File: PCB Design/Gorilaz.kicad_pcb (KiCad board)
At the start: 2 copper layers, 100 x 86 mm, 20 parts, among them J1 Conn_01x13, J2 Conn_01x13, J3 Conn_01x13, J4 Conn_01x13, J7 Conn_01x13, J8 Conn_01x13, M1 MountingHole_6.4mm_M6, M3 MountingHole_4.3mm_M4, M4 MountingHole_4.3mm_M4

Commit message: schema update
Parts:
- removed BZ1: Buzzer, Buzzer_Beeper:Buzzer_TDK_PS1240P02BT_D12.2mm_H6.5mm
- removed R1, R2, R3: R_US, Keebio-Parts:Resistor-Hybrid
- added C1: 100n, Capacitor_SMD:C_0402_1005Metric, F.Cu at (169.9, 119.6)
- added C17: 100n, Capacitor_SMD:C_0402_1005Metric, F.Cu at (124.0, 103.5)
- added C5: 4u7, Capacitor_SMD:C_0402_1005Metric, F.Cu at (125.5, 82.0)
- added C6: 4u7, Capacitor_SMD:C_0402_1005Metric, F.Cu at (129.3, 85.8)
- added C7: 4u7, Capacitor_SMD:C_0402_1005Metric, F.Cu at (120.0, 86.5)
- added C8: 100n, Capacitor_SMD:C_0402_1005Metric, F.Cu at (126.5, 113.0)
- added D2: LED_NUM, LED_SMD:LED_1206_3216Metric, F.Cu at (142.1, 140.0)
- added D3: LED_SCR, LED_SMD:LED_1206_3216Metric, F.Cu at (153.1, 140.5)
- added D5: BSD3C051V, Diode_SMD:D_SOD-323, F.Cu at (170.5, 122.0)
- added F1: 750 mA, Fuse:Fuse_0603_1608Metric, F.Cu at (160.5, 119.8)
- added J5: HRO_TYPE-C-31-M-14, Connector_USB:USB_C_Receptacle_HRO_TYPE-C-31-M-12, F.Cu at (165.2, 130.4)
- added J6: Battery, Local:Molex_Pico-EZmate_78171-0002_1x02-1MP_P1.20mm_Vertical, F.Cu at (125.2, 128.1)
- added J9: TC2030_SWD, Local:CON_TC2030_outlined, F.Cu at (156.4, 80.2)
- added L1: BLM15PX121SN1D, Inductor_SMD:L_0402_1005Metric, F.Cu at (160.5, 123.5)
- added L2: BLM15PX121SN1D, Inductor_SMD:L_0402_1005Metric, F.Cu at (170.0, 124.0)
- added LED2: orange, LED_SMD:LED_0402_1005Metric, F.Cu at (129.0, 91.5)
- added Q2: 2N7002, Package_TO_SOT_SMD:SOT-23, F.Cu at (130.9, 78.5)
- added R10: 1k5, Resistor_SMD:R_0402_1005Metric, F.Cu at (129.0, 89.0)
- added R11: 47k, Resistor_SMD:R_0402_1005Metric, F.Cu at (124.5, 82.0)
- added R12: 1k5, Resistor_SMD:R_0402_1005Metric, F.Cu at (129.5, 84.5)
- added R13: 3k9, Resistor_SMD:R_0402_1005Metric, F.Cu at (122.5, 82.0)
- added R15: 100R, Resistor_SMD:R_0402_1005Metric, F.Cu at (124.5, 122.5)
- added R17: 1k, Resistor_SMD:R_0402_1005Metric, F.Cu at (130.0, 121.0)
- added R18: 5k1, Resistor_SMD:R_0402_1005Metric, F.Cu at (131.5, 101.0)
- added R19: 5k1, Resistor_SMD:R_0402_1005Metric, F.Cu at (131.5, 103.0)
- added R20: 10k, Resistor_SMD:R_0805_2012Metric, F.Cu at (128.6, 136.5)
- added R21: 10k, Resistor_SMD:R_0805_2012Metric, F.Cu at (139.6, 136.5)
- added R22: 10k, Resistor_SMD:R_0805_2012Metric, F.Cu at (151.6, 137.5)
- added R5: 5k1, Resistor_SMD:R_0402_1005Metric, F.Cu at (166.8, 123.7)
- added R6: 10k, Resistor_SMD:R_0402_1005Metric, F.Cu at (127.9, 78.0)
- added R7: 100R, Resistor_SMD:R_0402_1005Metric, F.Cu at (125.9, 77.5)
- added R8: 100k, Resistor_SMD:R_0402_1005Metric, F.Cu at (132.0, 74.5)
- added R9: 10k, Resistor_SMD:R_0402_1005Metric, F.Cu at (120.0, 85.5)
- added SW1: PWR, Mastarlib:SW_MSK12C02-HB, F.Cu at (121.5, 57.5)
- added SW4: RST, Button_Switch_SMD:SW_SPST_SKQG_WithStem, F.Cu at (132.9, 58.1)
- added U1: SRV05-4, Package_TO_SOT_SMD:SOT-23-6, F.Cu at (164.6, 114.0)
- added U10: MAX17048, Local:DFN-8-1EP_2x2mm_P0.5mm_EP0.7x1.3mm, F.Cu at (127.5, 102.2)
- added U3: BQ24075, Package_DFN_QFN:VQFN-16-1EP_3x3mm_P0.5mm_EP1.6x1.6mm, F.Cu at (124.8, 86.1)
- added U4: DW01A, Package_TO_SOT_SMD:SOT-23-6, F.Cu at (127.0, 116.4)
- added U5: FS8205, Package_TO_SOT_SMD:SOT-23-6, F.Cu at (127.0, 122.4)
- added U8: nRF52840_moko_mk08, Mastarlib:nRF52840_moko_mk08, F.Cu at (169.6, 71.3)
- D1: footprint LED_THT:LED_D3.0mm -> LED_SMD:LED_1206_3216Metric
- D2, D3, D4, H1: moved to B.Cu
- H2, M1, M3, M4: moved to F.Cu
- J1, J2: footprint kinesisMod_board_connectors:Molex_0039532135 -> Local:Molex_0039532135; moved to F.Cu
- J3, J4: footprint kinesisMod_board_connectors:Molex_039532134 -> Local:Molex_0039532135; moved to F.Cu
- J7, J8: footprint kinx:39-53-2135 -> Local:Molex_0039532135; moved to F.Cu
- R4: value R_US -> 5k1; footprint Keebio-Parts:Resistor-Hybrid -> Resistor_SMD:R_0402_1005Metric; moved to F.Cu
- moved J3 88.7 mm to (106.0, 107.0)
- moved J4 86.8 mm to (190.0, 107.0)
- moved J1 84.8 mm to (106.0, 60.0)
- moved J2 83.1 mm to (190.0, 60.0)
- moved M3 81.7 mm to (107.5, 94.6), turned to 180 degrees
- moved M4 79.5 mm to (188.1, 94.6), turned to 180 degrees
- moved J7 73.1 mm to (112.0, 123.0)
- moved J8 71.6 mm to (184.0, 123.0)
- moved D4 28.5 mm to (134.1, 129.4), turned to 180 degrees
- moved D2 11.5 mm to (154.1, 129.4), turned to 180 degrees
- moved D1 10.6 mm to (133.6, 140.0)
- moved D3 8.48 mm to (144.1, 129.4), turned to 180 degrees
- moved R4 2.08 mm to (163.9, 123.7)
- moved H1 1.08 mm to (147.8, 103.0), turned to 180 degrees
- moved H2 1.08 mm to (147.8, 57.0), turned to 0 degrees
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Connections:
- net /COL_0 renamed col0
- net /COL_1 renamed col1
- net /COL_2 renamed col2
- net /COL_3 renamed col3
- net /COL_4 renamed col4
- net /COL_5 renamed col5
- net /COL_6 renamed col6
- net /ROW_12 renamed row12
- net /ROW_13 renamed row13
- net /ROW_14 renamed row14
- net /ROW_2 renamed row2
- net /ROW_3 renamed row3
- net /ROW_4 renamed row4
- net /ROW_5 renamed row5
- net /ROW_6 renamed row6
- net /ROW_7 renamed row7
- net /ROW_8 renamed row8
- net /ROW_9 renamed row9
- J3 pad 1: /ROW_10 -> row10
- J3 pad 8: /ROW_11 -> row11
- J4 pad 6: /ROW_0 -> row0
- J4 pad 7: /ROW_1 -> row1
- R4 pad 1: Net-(D4-A) -> GNDPWR
- R4 pad 2: /LED_KEYPAD -> Net-(J5-CC1)
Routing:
- net +BATT: track 0.00 -> 32.0 mm, vias 0 -> 2
- net GND: track 0.00 -> 17.8 mm
- net Net-(U4-VDD): track 0.00 -> 15.1 mm
- net SYSOFF: track 0.00 -> 14.5 mm, vias 0 -> 2
- net Net-(J6-Pin_2): track 0.00 -> 13.9 mm
- net USB-D+: track 0.00 -> 12.1 mm
- net USB-D-: track 0.00 -> 11.5 mm
- net SCL: track 0.00 -> 11.4 mm
- net VBUS: track 0.00 -> 11.2 mm
- net Earth: track 0.00 -> 10.2 mm
- net SDA: track 0.00 -> 9.99 mm
- net +5V: track 0.00 -> 8.71 mm
- net Net-(U4-CSI): track 0.00 -> 7.45 mm
- net +3.3V: track 0.00 -> 5.02 mm, vias 0 -> 2
- net Net-(D1-A): track 4.50 -> 0.00 mm
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
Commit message: v0
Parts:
- removed the D2 at (154.1, 129.4)
- removed the D3 at (144.1, 129.4)
- removed D4: LED_ALT, LED_THT:LED_D3.0mm
- removed J9: TC2030_SWD, Local:CON_TC2030_outlined
- D1, D2, D3: moved to B.Cu
- H1: moved to F.Cu
- moved SW4 36.0 mm to (157.8, 84.0)
- moved SW1 28.4 mm to (130.5, 84.4), turned to 90 degrees
- moved R20 22.3 mm to (141.4, 118.2)
- moved R15 22.0 mm to (130.2, 101.3)
- moved R17 22.0 mm to (135.7, 99.8)
- moved U5 22.0 mm to (132.7, 101.1)
- moved R21 21.8 mm to (151.4, 118.2)
- moved R22 21.7 mm to (161.4, 118.2)
- moved U4 20.8 mm to (132.6, 96.4)
- moved D3 20.5 mm to (161.3, 121.7), turned to 180 degrees
- moved D2 20.5 mm to (151.3, 121.7), turned to 180 degrees
- moved C8 20.4 mm to (132.2, 93.3)
- moved D1 19.9 mm to (141.3, 121.7), turned to 180 degrees
- moved R8 18.9 mm to (136.4, 92.9)
- moved U1 16.9 mm to (173.2, 99.5), turned to -90 degrees
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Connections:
- U8 pad 1: LED_CAPS_LOCK -> col5
- U8 pad 13: unconnected-(U8-P0.04-A-Pad13) -> LED_CAPS_LOCK
- U8 pad 14: unconnected-(U8-P0.06-Pad14) -> LED_NUM_LOCK
- U8 pad 15: unconnected-(U8-P0.11-Pad15) -> LED_SCROLL_LOCK
- U8 pad 16: unconnected-(U8-P0.08-Pad16) -> LED_KEYPAD
- U8 pad 17: unconnected-(U8-P0.09-LF-NFC-Pad17) -> col6
- U8 pad 18: unconnected-(U8-P0.10-LF-NFC-Pad18) -> col4
- U8 pad 2: LED_NUM_LOCK -> row10
- U8 pad 21: col0 -> col3
- U8 pad 22: col1 -> col2
- U8 pad 23: col2 -> col1
- U8 pad 24: col3 -> row0
- U8 pad 25: col4 -> row1
- U8 pad 26: col5 -> row2
- U8 pad 28: col6 -> row3
- U8 pad 29: unconnected-(U8-P0.20-Pad29) -> row4
- U8 pad 3: LED_SCROLL_LOCK -> row9
- U8 pad 30: unconnected-(U8-P0.21-Pad30) -> row5
- U8 pad 31: unconnected-(U8-P0.22-Pad31) -> row14
- U8 pad 32: unconnected-(U8-P0.23-Pad32) -> row13
- U8 pad 33: unconnected-(U8-P0.24-Pad33) -> col0
- U8 pad 34: unconnected-(U8-P0.25-Pad34) -> row12
- U8 pad 35: row0 -> unconnected-(U8-P1.10-LF-Pad35)
- U8 pad 36: row1 -> unconnected-(U8-P1.11-LF-Pad36)
- U8 pad 37: row2 -> unconnected-(U8-P1.12-LF-Pad37)
- U8 pad 38: row3 -> unconnected-(U8-P1.13-LF-Pad38)
- U8 pad 4: LED_KEYPAD -> row11
- U8 pad 40: row4 -> row6
- U8 pad 41: row5 -> unconnected-(U8-P1.15-LF-Pad41)
- U8 pad 44: row6 -> unconnected-(U8-P1.08-Pad44)
- U8 pad 45: row7 -> unconnected-(U8-P1.09-Pad45)
- U8 pad 5: unconnected-(U8-P0.30-LF-A-Pad5) -> row7
- U8 pad 50: row8 -> unconnected-(U8-P1.01-LF-Pad50)
- U8 pad 51: row9 -> unconnected-(U8-P1.02-LF-Pad51)
- U8 pad 52: row10 -> unconnected-(U8-P1.03-LF-Pad52)
- U8 pad 53: row11 -> unconnected-(U8-P1.04-LF-Pad53)
- U8 pad 54: row12 -> unconnected-(U8-P1.05-LF-Pad54)
- U8 pad 55: row13 -> unconnected-(U8-P1.06-LF-Pad55)
- U8 pad 56: row14 -> unconnected-(U8-P1.07-LF-Pad56)
- U8 pad 6: unconnected-(U8-P0.31-LF-A-Pad6) -> row8
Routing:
- net col5: track 0.00 -> 261.1 mm, vias 0 -> 3
- net col1: track 0.00 -> 171.3 mm, vias 0 -> 4
- net col2: track 0.00 -> 168.4 mm, vias 0 -> 4
- net col0: track 0.00 -> 168.3 mm, vias 0 -> 4
- net col4: track 0.00 -> 166.0 mm, vias 0 -> 4
- net col3: track 0.00 -> 162.8 mm, vias 0 -> 4
- net row14: track 0.00 -> 156.7 mm, vias 0 -> 8
- net row13: track 0.00 -> 153.9 mm, vias 0 -> 6
- net row12: track 0.00 -> 129.1 mm, vias 0 -> 2
- net col6: track 0.00 -> 123.5 mm, vias 0 -> 1
- net row6: track 0.00 -> 93.8 mm, vias 0 -> 2
- net row7: track 0.00 -> 90.0 mm, vias 0 -> 1
- net row9: track 0.00 -> 89.4 mm, vias 0 -> 1
- net row8: track 0.00 -> 89.3 mm, vias 0 -> 1
- net row11: track 0.00 -> 74.5 mm
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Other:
- board text added: "Gorillaz Board V0 Feb 2026 https://github.com/nol00p/Gorillaz"
- board text removed: "CAPSLCK"
- board text removed: "KB600"
- board text removed: "Molex 39-53-2135"
- board text removed: "Top Left of Board X: 100 Y: 50"

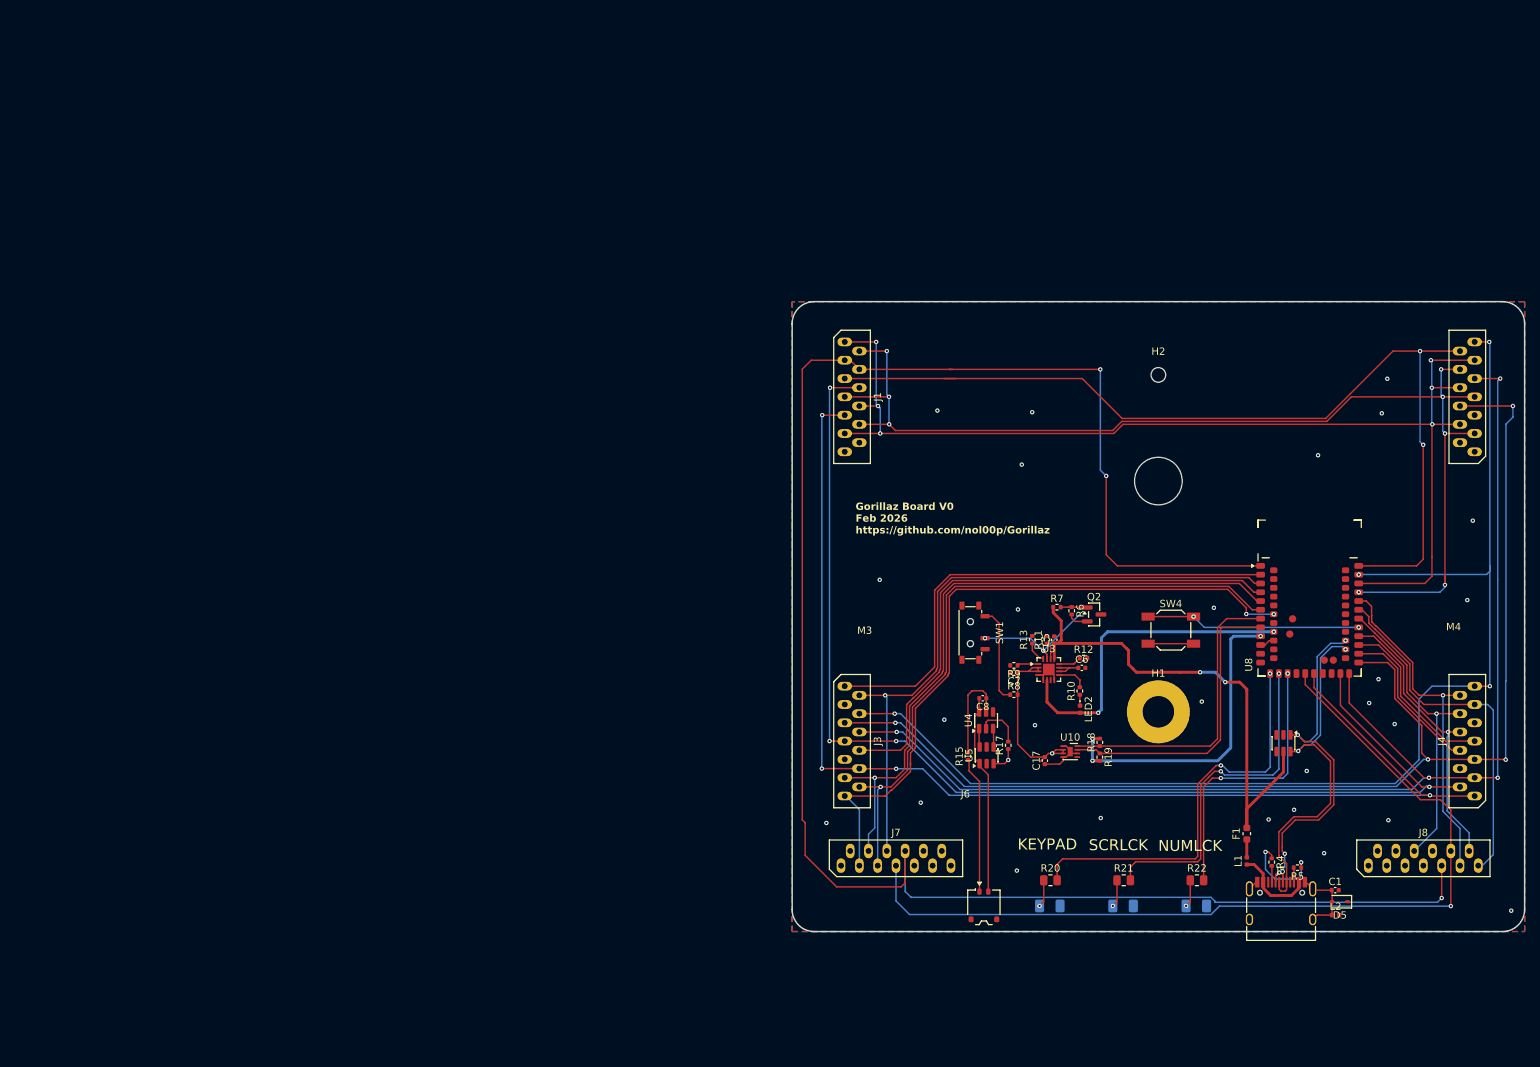
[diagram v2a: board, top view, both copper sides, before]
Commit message: Data lane correction
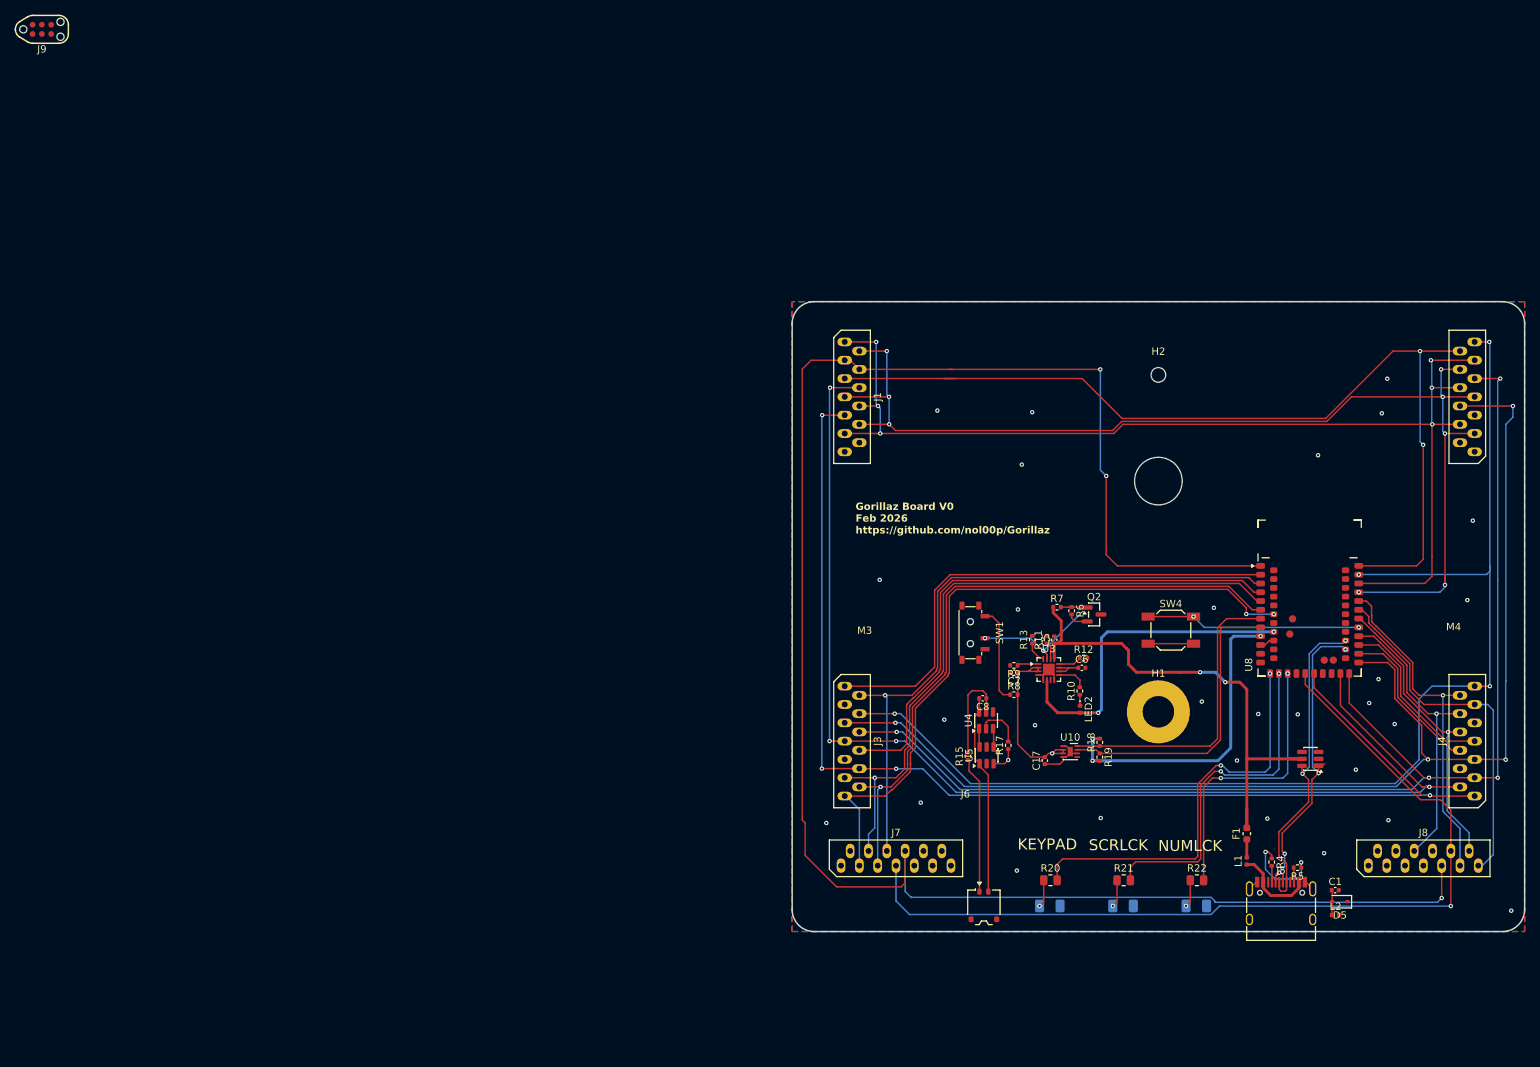
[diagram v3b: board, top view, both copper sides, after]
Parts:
- added J9: TC2030_SWD, Local:CON_TC2030_outlined, F.Cu at (3.72, 2.02)
- moved U1 4.24 mm to (176.9, 101.6), turned to 180 degrees
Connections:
- J5 pad B1: Earth -> GND
- J5 pad B12: Earth -> GND
- J5 pad S1: Earth -> GND
- U8 pad 47: USB-D+ -> USB-D-
- U8 pad 48: USB-D- -> USB-D+
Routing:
- net USB-D-: track 50.0 -> 43.5 mm
- net USB-D+: track 50.4 -> 44.0 mm
- net Earth: track 12.0 -> 6.67 mm
- net +5V: track 69.7 -> 69.2 mm
- net GND: vias 28 -> 30

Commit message: USB-C update
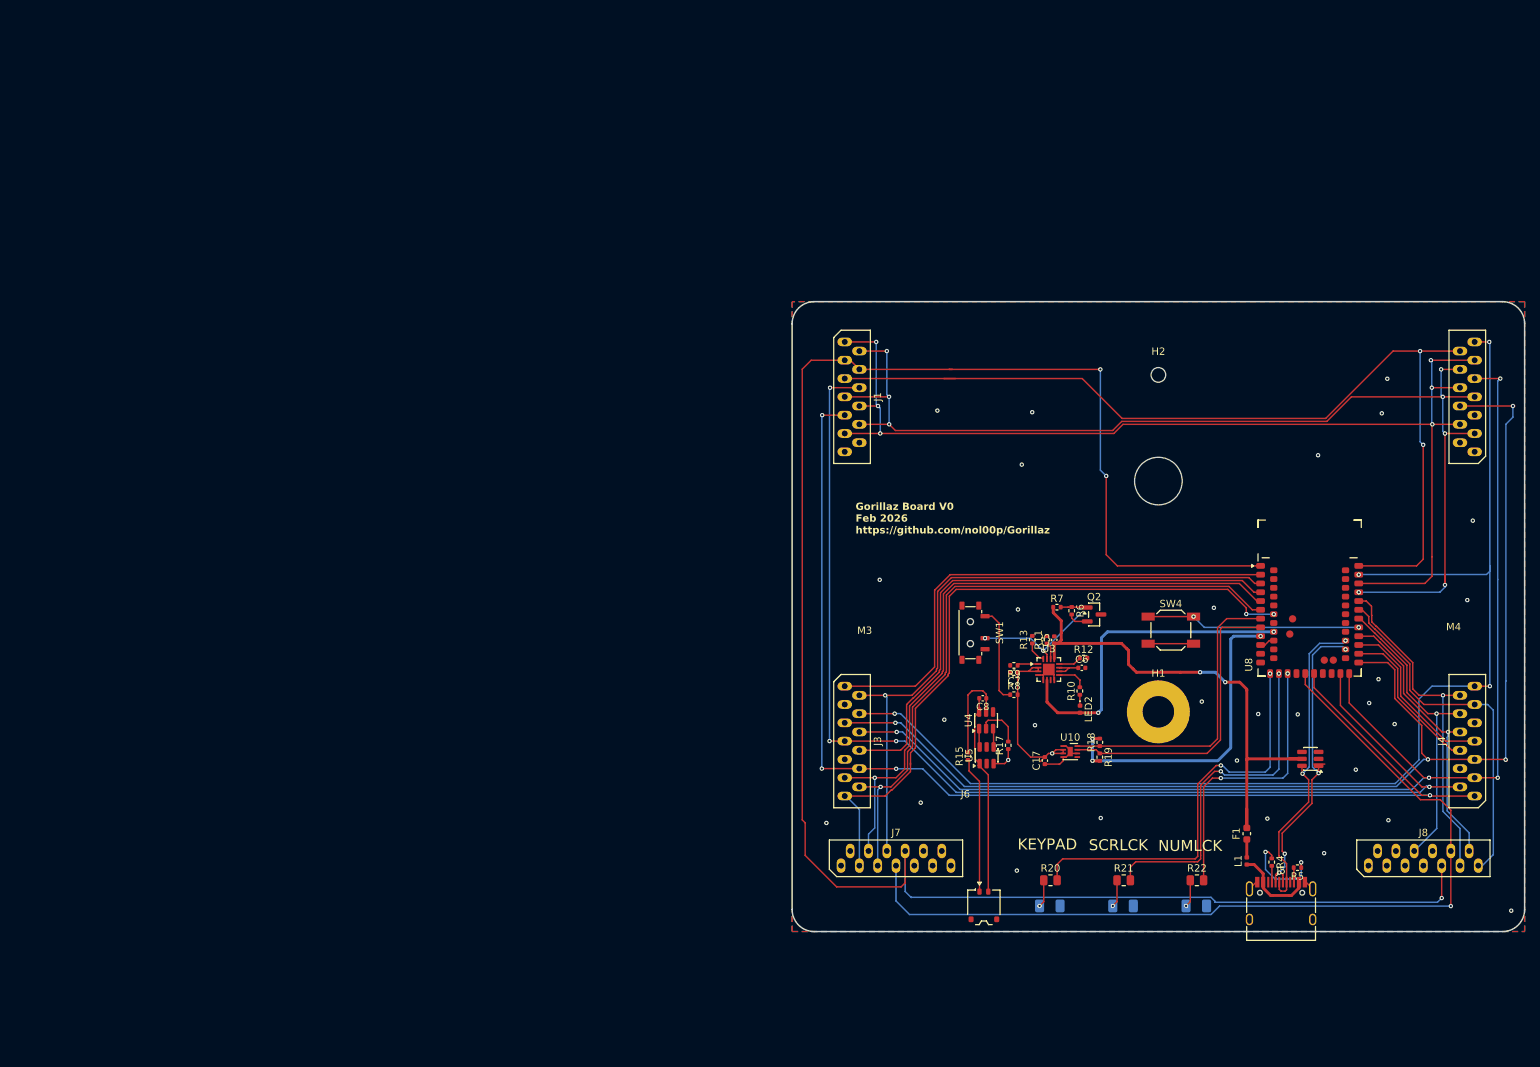
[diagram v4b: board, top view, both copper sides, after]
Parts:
- removed C1: 100n, Capacitor_SMD:C_0402_1005Metric
- removed D5: BSD3C051V, Diode_SMD:D_SOD-323
- removed J9: TC2030_SWD, Local:CON_TC2030_outlined
- removed L2: BLM15PX121SN1D, Inductor_SMD:L_0402_1005Metric
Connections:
- J5 pad A1: Earth -> GND
- J5 pad A12: Earth -> GND
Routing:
- net Earth: track 6.67 -> 0.00 mm
- net GND: track 26.0 -> 29.2 mm

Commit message: power managemnt rework
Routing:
- net GND: track 29.2 -> 30.6 mm, vias 30 -> 32
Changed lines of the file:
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@@
 	(segment
 		(start 140.43622 90.172879)
-		(end 141.18622 89.422879)
+		(end 141.11705 89.49205)
 		(width 0.2)
 		(layer "F.Cu")
@@
 	)
 	(segment
+		(start 141.11705 89.49205)
+		(end 141.18622 89.422879)
+		(width 0.2)
+		(layer "F.Cu")
+		(net 5)
+	)
+	(segment
 		(start 169.495 118.455)
 		(end 168.58 119.37)
@@
 	)
 	(segment
+		(start 132.4825 86.65)
+		(end 133.125 87.2925)
+		(width 0.2)
+		(layer "F.Cu")
+		(net 5)
+	)
+	(segment
 		(start 140.43622 90.860379)
 		(end 140.43622 90.172879)
@@
 	)
 	(segment
+		(start 133.125 87.2925)
+		(end 133.125 87.85)
+		(width 0.2)
+		(layer "F.Cu")
+		(net 5)
+	)
+	(segment
 		(start 144.3625 100.88)
 		(end 144.1125 100.63)
@@
 	)
 	(via
+		(at 141.11705 89.49205)
+		(size 0.6)
+		(drill 0.3)
+		(layers "F.Cu" "B.Cu")
+		(net 5)
+	)
+	(via
 		(at 198.325 79.95)
 		(size 0.6)
@@
 		(net 5)
 	)
+	(via
+		(at 133.125 87.85)
+		(size 0.6)
+		(drill 0.3)
+		(layers "F.Cu" "B.Cu")
+		(net 5)
+	)
